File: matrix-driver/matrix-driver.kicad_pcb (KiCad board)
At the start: 4 copper layers, 35 parts, among them IC1 SPX5205M5-L-3-3_TR, J1 Conn_01x09, J2 Conn_01x08, J3 Conn_01x27, J4 Conn_01x27, J5 Conn_01x08, U1 TPS562202, U2 LP5891MRRFR, U3 TPS562202

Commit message: added gerbers and finalized v1.0
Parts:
- removed C15, C16: 0.1uF, Capacitor_SMD:C_0402_1005Metric
- added H1: MountingHole, MountingHole:MountingHole_3.2mm_M3_DIN965, F.Cu at (100.0, 98.0)
- added H2: MountingHole, MountingHole:MountingHole_3.2mm_M3_DIN965, F.Cu at (170.0, 98.0)
- added H3: MountingHole, MountingHole:MountingHole_3.2mm_M3_DIN965, F.Cu at (100.0, 138.0)
- added H4: MountingHole, MountingHole:MountingHole_3.2mm_M3_DIN965, F.Cu at (170.0, 138.0)
- added L1: 4.7uH, ETQ_P3M3R3KVP:IND_PCC-M0530M-LP_PAN, F.Cu at (145.4, 118.8)
- added L2: 3.3uH, ETQ_P3M3R3KVP:IND_PCC-M0530M-LP_PAN, F.Cu at (145.4, 130.8)
- C12, C13: value 22uF -> 33uF
- C14: value 10nF -> 10pF
- C7: value 10nF -> 22pF
- moved J4 80.7 mm to (115.0, 133.5)
- moved R4 54.0 mm to (146.2, 140.2), turned to 180 degrees
- moved R5 48.9 mm to (152.0, 139.7), turned to 180 degrees
- moved R6 46.1 mm to (149.7, 138.2), turned to 90 degrees
- moved C8 42.4 mm to (146.2, 138.7)
- moved J2 38.6 mm to (117.0, 101.4)
- moved C1 38.4 mm to (146.2, 126.8)
- moved R1 35.8 mm to (150.5, 131.6), turned to 180 degrees
- moved C11 35.3 mm to (149.7, 134.9), turned to -90 degrees
- moved C14 35.2 mm to (152.0, 138.1), turned to 180 degrees
- moved J1 34.7 mm to (164.5, 118.8), turned to 90 degrees
- moved C7 34.2 mm to (151.3, 129.3), turned to 90 degrees
- moved R2 31.9 mm to (149.7, 129.3), turned to 90 degrees
- moved C4 31.0 mm to (149.7, 122.8), turned to -90 degrees
- moved C2 30.8 mm to (154.1, 122.8), turned to -90 degrees
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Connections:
- C17 pad 1: Net-(IC1-EN) -> +12V
- IC1 pad 1: Net-(IC1-EN) -> +12V
- IC1 pad 3: Net-(IC1-EN) -> +12V
- J3 pad 25: +3.3V -> +3V3
- J4 pad 25: +3.3V -> +3V3
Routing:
- net +3V3: track 0.00 -> 61.5 mm, vias 0 -> 5
- net /R15: track 0.00 -> 54.8 mm, vias 0 -> 2
- net /G15: track 0.00 -> 52.2 mm, vias 0 -> 2
- net /B15: track 0.00 -> 47.5 mm, vias 0 -> 2
- net /B14: track 0.00 -> 46.8 mm, vias 0 -> 2
- net /R14: track 0.00 -> 45.9 mm, vias 0 -> 2
- net /G14: track 0.00 -> 45.8 mm, vias 0 -> 2
- net /2V8_EN: track 0.00 -> 42.6 mm, vias 0 -> 2
- net /G13: track 0.00 -> 40.0 mm, vias 0 -> 2
- net /SOUT: track 0.00 -> 39.1 mm, vias 0 -> 2
- net /SIN: track 0.00 -> 37.5 mm, vias 0 -> 2
- net /R13: track 0.00 -> 36.6 mm, vias 0 -> 2
- net /R12: track 0.00 -> 35.1 mm, vias 0 -> 2
- net /B12: track 0.00 -> 34.9 mm, vias 0 -> 2
- net /B13: track 0.00 -> 34.8 mm
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- added copper zone on F.Cu, net +12V
- added copper zone on F.Cu, net +2V8
- added copper zone on In2.Cu, net +2V8
- added copper zone on F.Cu, net +3V8
- added copper zone on B.Cu, net GND
- added copper zone on F.Cu, net GND
- added copper zone on In1.Cu, net GND
- added copper zone on In2.Cu, net GND
- added copper zone on F.Cu, net Net-(U1-SW)
- added copper zone on F.Cu, net Net-(U3-SW)
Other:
- board outline added: 76 x 50 mm
- board text added: "0-7"
- board text added: "11V-17V"
- board text added: "8-15"
- board text added: "MatrixDrive"
- board text added: "VG/VB ADJ"
- board text added: "VR ADJ"
- board text added: "v1.0"

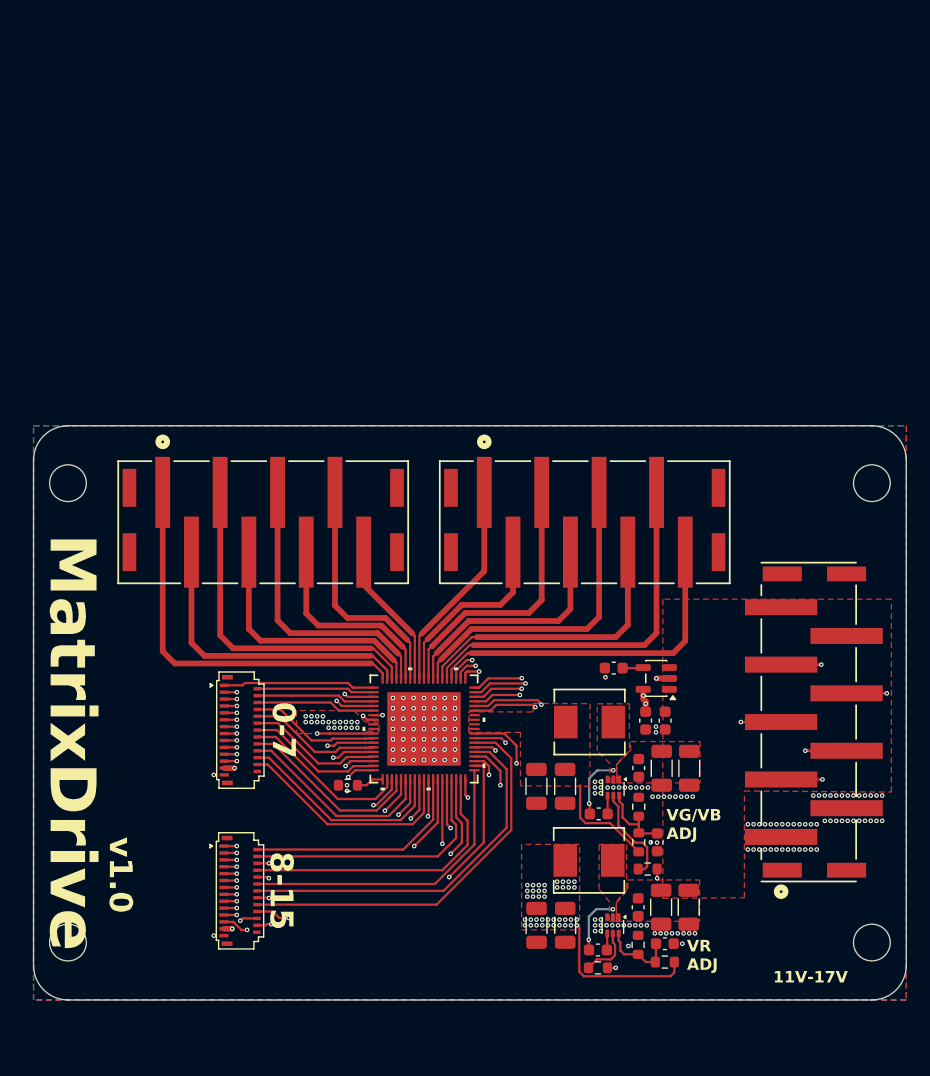
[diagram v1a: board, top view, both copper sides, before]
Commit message: changed to through hole connectors for matrix drive unit and updated schematic to reflect thermistors and reserved pin
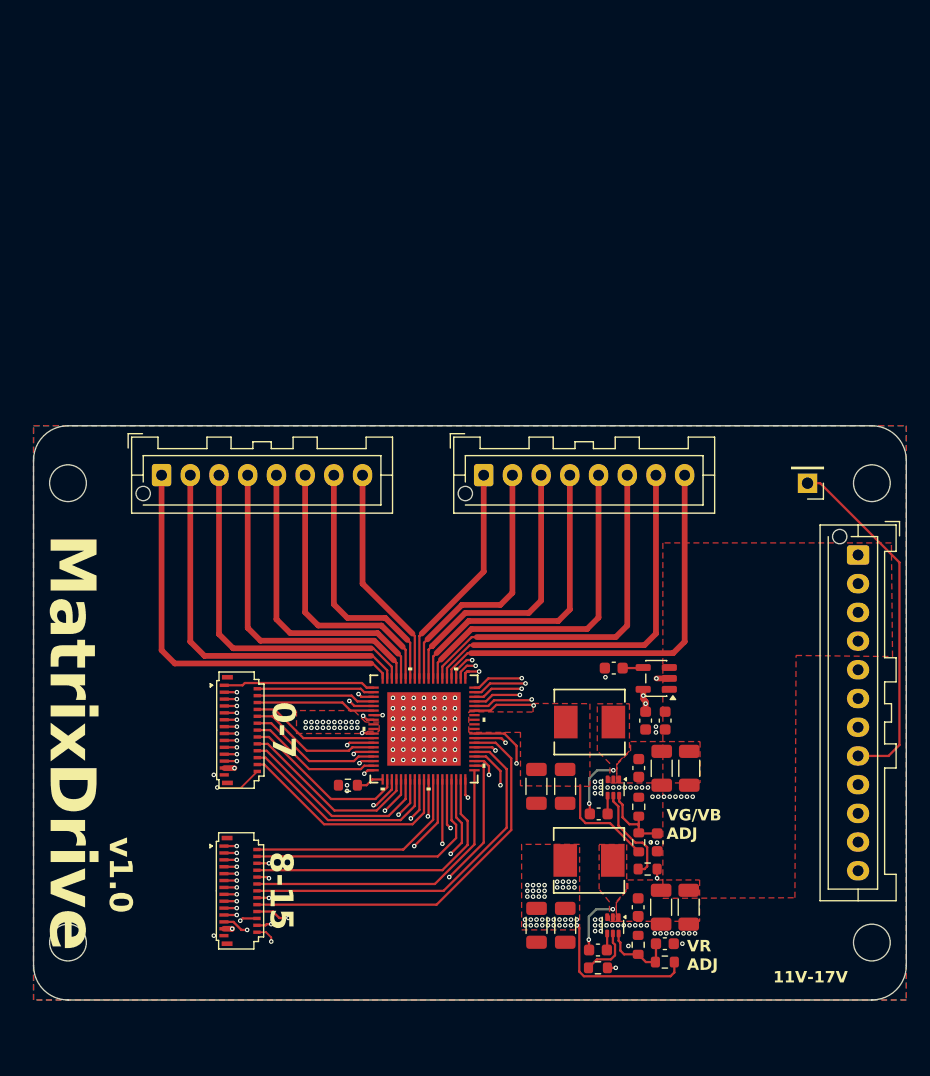
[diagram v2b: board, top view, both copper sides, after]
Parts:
- added J2: Conn_01x12, Connector_JST:JST_XA_B12B-XASK-1-A_1x12_P2.50mm_Vertical, F.Cu at (168.8, 104.2)
- J1: value Conn_01x09 -> Conn_01x01; footprint CONN_BM09B-XASS-TF_JST:CONN_BM09B-XASS-TF_JST -> Connector_PinHeader_2.54mm:PinHeader_1x01_P2.54mm_Vertical
- J5: renamed from J2; footprint CONN_BM08B-XASS-TF_JST:CONN_BM08B-XASS-TF_JST -> Connector_JST:JST_XA_B08B-XASK-1-A_1x08_P2.50mm_Vertical
- J6: renamed from J5; footprint CONN_BM08B-XASS-TF_JST:CONN_BM08B-XASS-TF_JST -> Connector_JST:JST_XA_B08B-XASK-1-A_1x08_P2.50mm_Vertical
- moved J1 20.8 mm to (164.4, 98.0), turned to 180 degrees
- moved J5 9.75 mm to (108.2, 97.3)
- moved J6 9.71 mm to (136.2, 97.3)
- renumbered C2 to C1, C8 to C10, C7 to C11, C14 to C12, C19 to C13, C5 to C14, C12 to C15, C6 to C16, C13 to C17, C9 to C2, C10 to C4, C4 to C5, C11 to C6, C17 to C7, C18 to C8, C1 to C9, R7 to R1, R1 to R2, R4 to R3, R2 to R4, R3 to R5, R5 to R6, R6 to R7, U2 to U1, U1 to U2
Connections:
- J1 pad 1: +12V -> Net-(J1-Pin_1)
- J3 pad 26: /interconnect/TH1 -> /TH1
- J4 pad 26: /interconnect/TH2 -> /TH2
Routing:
- net /TH1: track 0.00 -> 81.6 mm, vias 0 -> 1
- net /TH2: track 0.00 -> 57.5 mm, vias 0 -> 1
- net Net-(J1-Pin_1): track 0.00 -> 30.8 mm
- net /LINE5: track 17.8 -> 24.6 mm
- net /LINE7: track 12.8 -> 19.6 mm
- net /LINE3: track 22.1 -> 28.9 mm
- net /LINE1: track 26.6 -> 33.4 mm
- net /LINE13: track 25.0 -> 31.7 mm
- net /LINE9: track 16.2 -> 22.8 mm
- net /LINE15: track 29.9 -> 36.6 mm
- net /LINE11: track 20.5 -> 27.2 mm
- net /SCLK: track 31.6 -> 36.4 mm, vias 2 -> 1
- net /SOUT: track 39.1 -> 36.7 mm, vias 2 -> 1
- net /3V8_EN: track 28.8 -> 31.2 mm, vias 2 -> 1
- net /LINE2: track 29.5 -> 31.1 mm
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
